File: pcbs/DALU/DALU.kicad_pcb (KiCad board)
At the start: 2 copper layers, 55 parts, among them J201 Conn_02x20_Odd_Even, U201 74HC245, U202 74HC245, U203 74HC245, U301 74HC86, U302 74HC125, U303 74HC86, U304 74HC86, U305 74HC283, U306 74HC283, U307 74HC245, U401 74HC00, U402 74HC00, U403 74HC245, U404 74HC245, U501 74HC86, U502 74HC86, U503 74HC245, U601 74HC245, U701 74HC74, U702 74HC125, U703 74HCT574

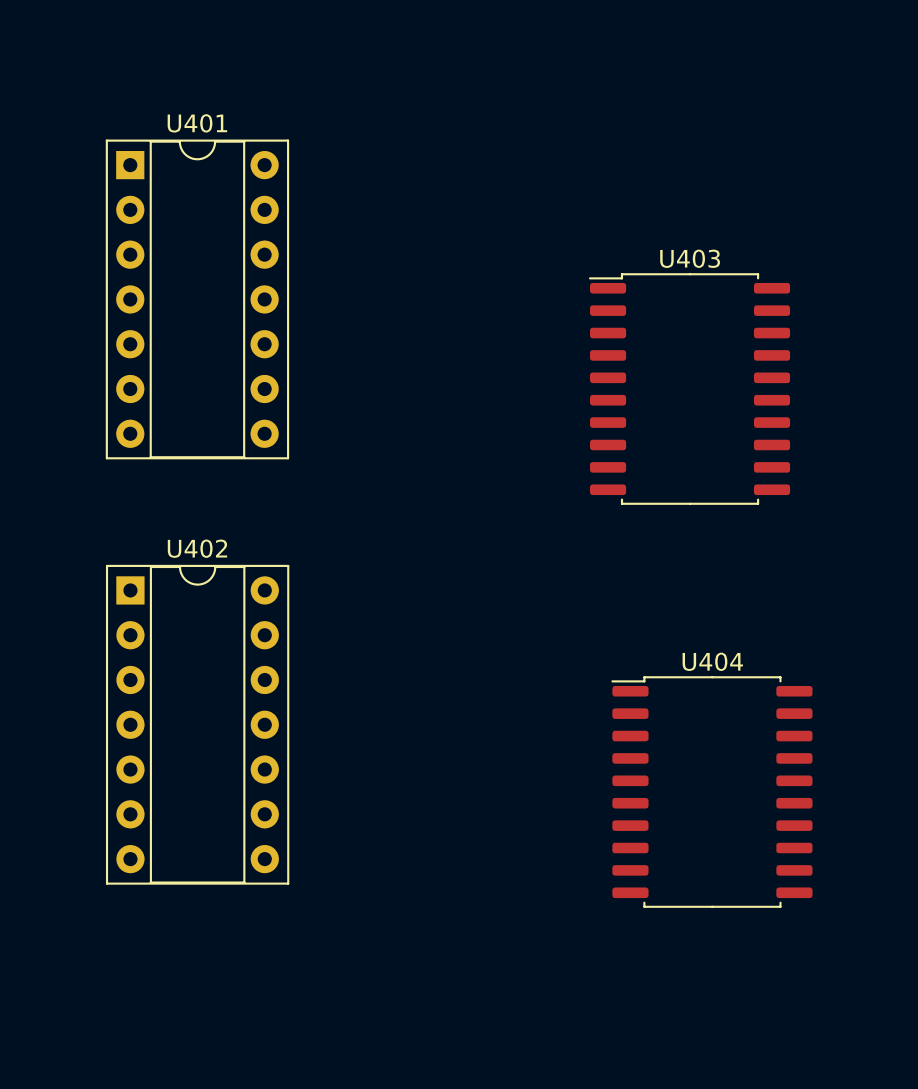
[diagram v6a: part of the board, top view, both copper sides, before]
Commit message: Input stage fiddling
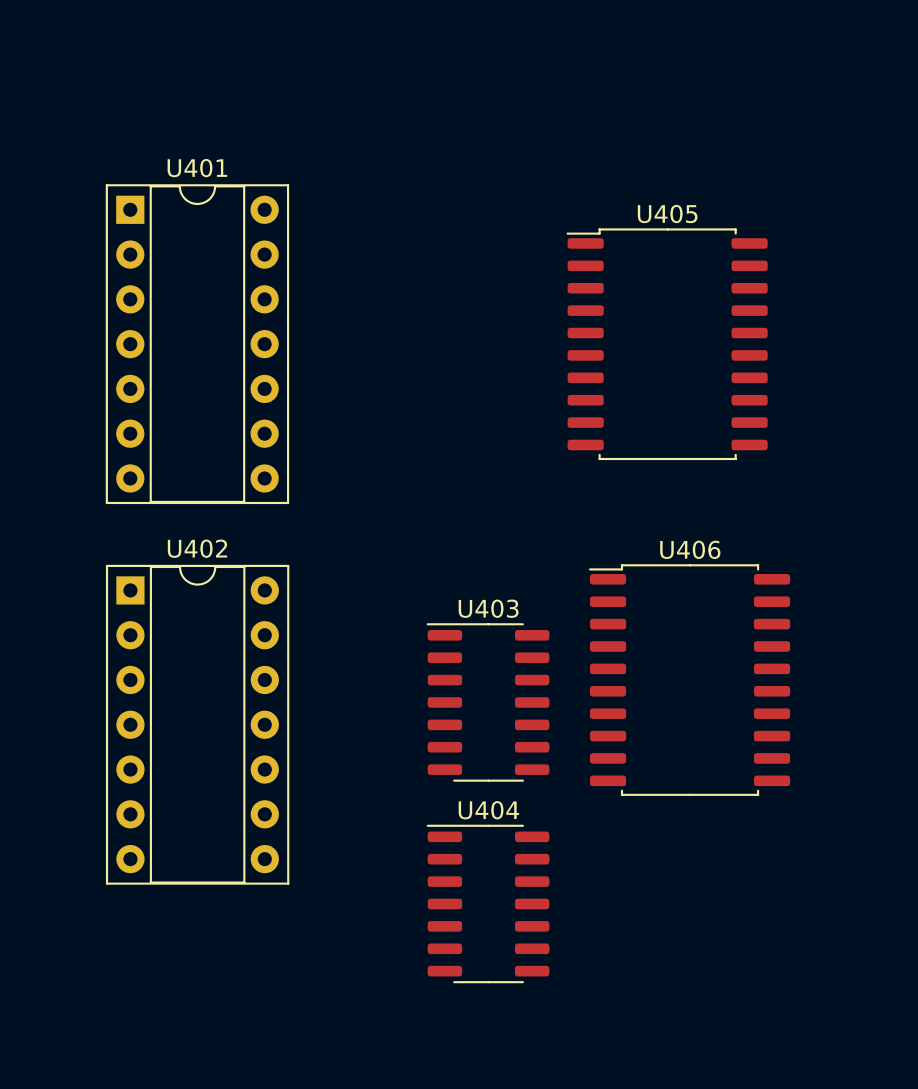
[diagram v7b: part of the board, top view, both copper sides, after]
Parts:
- added U403: 74HC14, Package_SO:SOIC-14_3.9x8.7mm_P1.27mm, F.Cu at (123.2, 132.1)
- added U404: 74HC14, Package_SO:SOIC-14_3.9x8.7mm_P1.27mm, F.Cu at (123.2, 143.5)
- moved U406 6.48 mm to (134.6, 130.8)
- moved U405 2.84 mm to (133.3, 111.8)
- moved U401 2.54 mm to (102.9, 104.1)
- renumbered U403 to U405, U404 to U406
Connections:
- U406 pad 2: unconnected-(U404-Pad2) -> Net-(U406-Pad2)
- U406 pad 3: unconnected-(U404-Pad3) -> Net-(U406-Pad3)
- U406 pad 4: unconnected-(U404-Pad4) -> Net-(U406-Pad4)
- U406 pad 5: unconnected-(U404-Pad5) -> Net-(U406-Pad5)
- U406 pad 6: unconnected-(U404-Pad6) -> Net-(U406-Pad6)
- U406 pad 7: unconnected-(U404-Pad7) -> Net-(U406-Pad7)
- U406 pad 8: unconnected-(U404-Pad8) -> Net-(U406-Pad8)
- U406 pad 9: unconnected-(U404-Pad9) -> Net-(U406-Pad9)

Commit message: Starting to think about decoding etc.
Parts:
- removed the D701 at (262.9, 20.3)
- removed the D702 at (262.9, 25.4)
- removed R301: 100k, Resistor_THT:R_Axial_DIN0207_L6.3mm_D2.5mm_P7.62mm_Horizontal
- removed the R701 at (265.4, 20.3)
- removed the R702 at (293.4, 47.0)
- removed the R703 at (262.9, 30.5)
- removed the R704 at (275.6, 35.6)
- removed U302, U702: 74HC125, Package_DIP:DIP-14_W7.62mm_Socket
- removed U304: 74HC86, Package_DIP:DIP-14_W7.62mm_Socket
- added D301: LED, LED_SMD:LED_0603_1608Metric, F.Cu at (40.6, 176.5)
- added D302: LED, LED_SMD:LED_0603_1608Metric, F.Cu at (40.6, 179.1)
- added D303: LED, LED_SMD:LED_0603_1608Metric, F.Cu at (40.6, 181.6)
- added D304: LED, LED_SMD:LED_0603_1608Metric, F.Cu at (40.6, 184.2)
- added D305: LED, LED_SMD:LED_0603_1608Metric, F.Cu at (76.2, 179.1)
- added D306: LED, LED_SMD:LED_0603_1608Metric, F.Cu at (76.2, 181.6)
- added D307: LED, LED_SMD:LED_0603_1608Metric, F.Cu at (76.2, 184.2)
- added D308: LED, LED_SMD:LED_0603_1608Metric, F.Cu at (76.2, 186.7)
- added D309: LED, LED_SMD:LED_0603_1608Metric, F.Cu at (76.2, 168.9)
- added D310: LED, LED_SMD:LED_0603_1608Metric, F.Cu at (76.2, 171.4)
- added D311: LED, LED_SMD:LED_0603_1608Metric, F.Cu at (76.2, 174.0)
- added D312: LED, LED_SMD:LED_0603_1608Metric, F.Cu at (76.2, 176.5)
- added RN201: 10k, Resistor_SMD:R_Array_Convex_4x0402, F.Cu at (71.1, 142.2)
- added RN202: 10k, Resistor_SMD:R_Array_Convex_4x0402, F.Cu at (71.1, 147.3)
- added RN301: 4k7, Resistor_SMD:R_Array_Convex_4x0603, F.Cu at (34.3, 180.3)
- added RN302: 4k7, Resistor_SMD:R_Array_Convex_4x0603, F.Cu at (83.3, 182.4)
- added RN303: 4k7, Resistor_SMD:R_Array_Convex_4x0603, F.Cu at (83.3, 177.6)
- added U301: 74HC138, Package_DIP:DIP-16_W7.62mm_Socket, F.Cu at (57.1, 166.4)
- added U403: 74HC86, Package_DIP:DIP-14_W7.62mm_Socket, F.Cu at (119.4, 30.5)
- moved U802 16.7 mm to (298.5, 3.81)
- renumbered D601 to D701, D602 to D702, D603 to D703, D604 to D704, D605 to D705, D606 to D706, D607 to D707, D608 to D708, D609 to D709, D610 to D710, D611 to D711, D612 to D712, D613 to D713, D614 to D714, D615 to D715, D616 to D716, R601 to R701, R602 to R702, R603 to R703, R604 to R704, R605 to R705, R606 to R706, R607 to R707, R608 to R708, R705 to R801, RN701 to RN801, U301 to U401, U303 to U402, U305 to U404, U306 to U405, U307 to U406, U401 to U501, U402 to U502, U403 to U503, U404 to U504, U405 to U505, U406 to U506, U501 to U601, U502 to U602, U503 to U603, U601 to U701, U701 to U801, U703 to U802
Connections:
- net Net-(J201-Pad18) renamed /Connector/A^{raw}_{0}
- net Net-(J201-Pad38) renamed /Connector/B^{raw}_{0}
- U201 pad 10: unconnected-(U201-Pad10) -> GND
- U201 pad 19: unconnected-(U201-Pad19) -> /Connector/~{SELECT_{DALU}}
- U202 pad 10: unconnected-(U202-Pad10) -> GND
- U202 pad 11: unconnected-(U202-Pad11) -> /Connector/A0
- U202 pad 12: unconnected-(U202-Pad12) -> /Connector/A1
- U202 pad 13: unconnected-(U202-Pad13) -> /Connector/A2
- U202 pad 14: unconnected-(U202-Pad14) -> /Connector/A3
- U202 pad 15: unconnected-(U202-Pad15) -> /Connector/A4
- U202 pad 16: unconnected-(U202-Pad16) -> /Connector/A5
- U202 pad 17: unconnected-(U202-Pad17) -> /Connector/A6
- U202 pad 18: unconnected-(U202-Pad18) -> /Connector/A7
- U202 pad 19: unconnected-(U202-Pad19) -> GND
- U203 pad 10: unconnected-(U203-Pad10) -> GND
- U203 pad 11: unconnected-(U203-Pad11) -> /Connector/B0
- U203 pad 12: unconnected-(U203-Pad12) -> /Connector/B1
- U203 pad 13: unconnected-(U203-Pad13) -> /Connector/B2
- U203 pad 14: unconnected-(U203-Pad14) -> /Connector/B3
- U203 pad 15: unconnected-(U203-Pad15) -> /Connector/B4
- U203 pad 16: unconnected-(U203-Pad16) -> /Connector/B5
- U203 pad 17: unconnected-(U203-Pad17) -> /Connector/B6
- U203 pad 18: unconnected-(U203-Pad18) -> /Connector/B7
- U203 pad 19: unconnected-(U203-Pad19) -> GND
- U404 pad 12: /AdderSubtractor/A3 -> /AND-NAND/A3
- U404 pad 14: /AdderSubtractor/A2 -> /AND-NAND/A2
- U404 pad 3: /AdderSubtractor/A1 -> /AND-NAND/A1
- U404 pad 5: /AdderSubtractor/A0 -> /AND-NAND/A0
- U405 pad 12: /AdderSubtractor/A7 -> /AND-NAND/A7
- U405 pad 14: /AdderSubtractor/A6 -> /AND-NAND/A6
- U405 pad 3: /AdderSubtractor/A5 -> /AND-NAND/A5
- U405 pad 5: /AdderSubtractor/A4 -> /AND-NAND/A4
- U802 pad 1: Net-(R704-Pad2) -> unconnected-(U802-Pad1)
